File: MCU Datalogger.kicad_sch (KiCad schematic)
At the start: 25 parts, among them U1 24LC1025, U2 24LC1025, U3 ATMEGA328P-AU, U4 DS1337S_, Y1 32.768kHz, Y2 16KHz

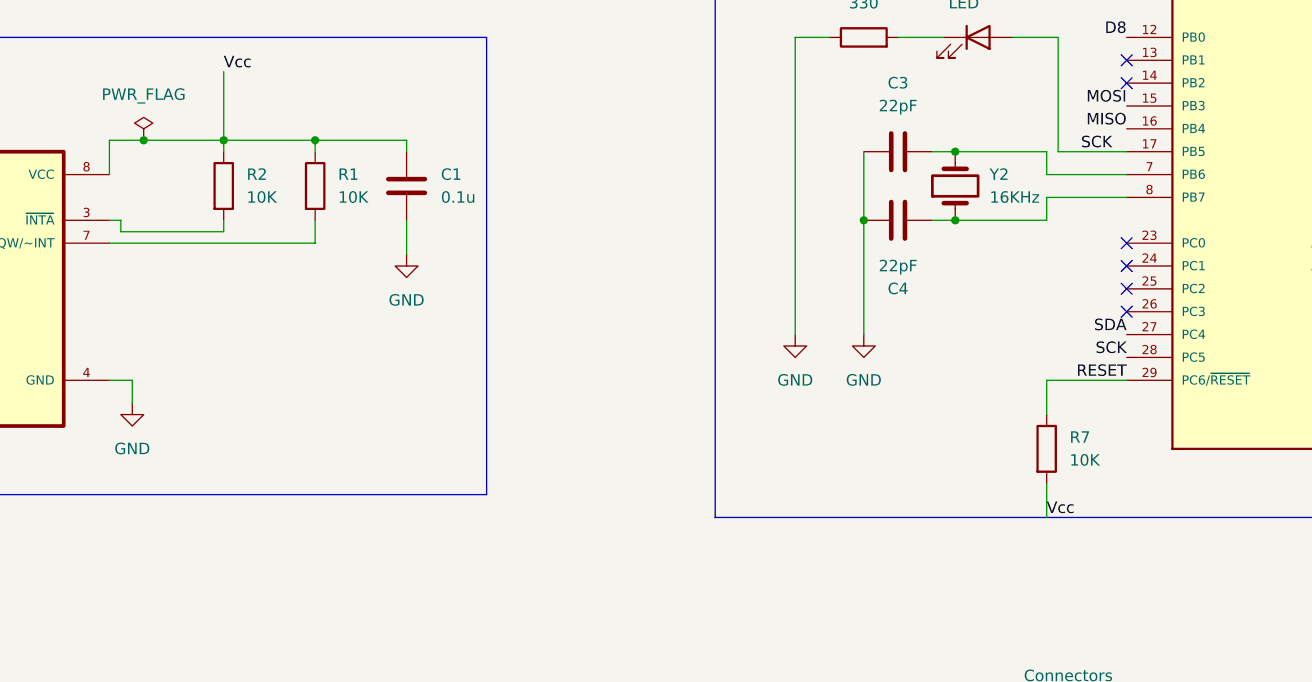
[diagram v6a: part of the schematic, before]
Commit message: completed the routing of the PCB
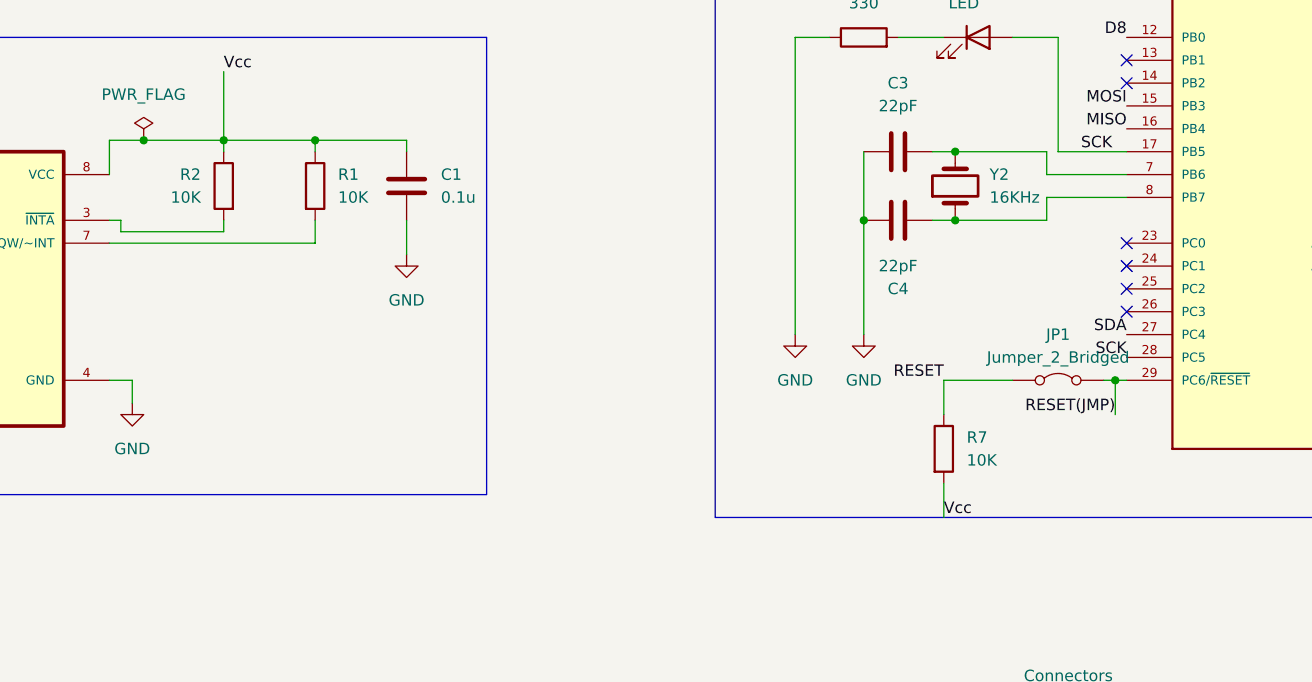
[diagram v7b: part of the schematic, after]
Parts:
- added JP1: Jumper_2_Bridged, Resistor_SMD:R_1206_3216Metric_Pad1.30x1.75mm_HandSolder, symbol Jumper:Jumper_2_Bridged
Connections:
- net RESET: now also JP1.2 (B); no longer U3.29 (PC6/~{RESET})
- new net RESET(JMP): JP1.1 (A), U3.29 (PC6/~{RESET})
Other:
- moved on the sheet: R7
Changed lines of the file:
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@@
 	)
 	(junction
+		(at 199.39 81.28)
+		(diameter 0)
+		(color 0 0 0 0)
+	)
+	(junction
 		(at 273.05 57.15)
 		(diameter 0)
@@
 	(wire
 		(pts
-			(xy 191.77 81.28) (xy 191.77 85.09)
-		)
-		(stroke
-			(width 0)
-			(type default)
-		)
-	)
-	(wire
-		(pts
 			(xy 124.46 151.13) (xy 130.81 151.13)
 		)
@@
 	(wire
 		(pts
+			(xy 199.39 81.28) (xy 200.66 81.28)
+		)
+		(stroke
+			(width 0)
+			(type default)
+		)
+	)
+	(wire
+		(pts
 			(xy 171.45 119.38) (xy 171.45 123.19)
 		)
@@
 	(wire
 		(pts
+			(xy 180.34 81.28) (xy 180.34 85.09)
+		)
+		(stroke
+			(width 0)
+			(type default)
+		)
+	)
+	(wire
+		(pts
 			(xy 181.61 63.5) (xy 191.77 63.5)
 		)
@@
 	(wire
 		(pts
+			(xy 198.12 81.28) (xy 199.39 81.28)
+		)
+		(stroke
+			(width 0)
+			(type default)
+		)
+	)
+	(wire
+		(pts
 			(xy 231.14 86.36) (xy 238.76 86.36)
 		)
@@
 	(wire
 		(pts
-			(xy 191.77 92.71) (xy 191.77 96.52)
+			(xy 180.34 92.71) (xy 180.34 96.52)
 		)
 		(stroke
@@
 	(wire
 		(pts
+			(xy 199.39 85.09) (xy 199.39 81.28)
+		)
+		(stroke
+			(width 0)
+			(type default)
+		)
+	)
+	(wire
+		(pts
 			(xy 273.05 86.36) (xy 273.05 57.15)
 		)
@@
 	(wire
 		(pts
+			(xy 187.96 81.28) (xy 180.34 81.28)
+		)
+		(stroke
+			(width 0)
+			(type default)
+		)
+	)
+	(wire
+		(pts
 			(xy 181.61 55.88) (xy 191.77 55.88)
 		)
@@
 	(wire
 		(pts
-			(xy 200.66 81.28) (xy 191.77 81.28)
-		)
-		(stroke
-			(width 0)
-			(type default)
-		)
-	)
-	(wire
-		(pts
 			(xy 90.17 81.28) (xy 90.17 83.82)
 		)
@@
 		)
 	)
-	(label "D8"
-		(at 200.66 43.18 180)
+	(label "RESET(JMP)"
+		(at 199.39 85.09 180)
 		(fields_autoplaced yes)
 		(effects
@@
 		)
 	)
-	(label "Vcc"
-		(at 191.77 96.52 0)
+	(label "D8"
+		(at 200.66 43.18 180)
 		(fields_autoplaced yes)
 		(effects
@@
 				(size 1.27 1.27)
 			)
-			(justify left bottom)
+			(justify right bottom)
 		)
 	)
-	(label "RESET"
-		(at 200.66 81.28 180)
+	(label "Vcc"
+		(at 180.34 96.52 0)
 		(fields_autoplaced yes)
 		(effects
@@
 				(size 1.27 1.27)
 			)
-			(justify right bottom)
+			(justify left bottom)
 		)
 	)
@@
 		)
 	)
+	(label "RESET"
+		(at 180.34 81.28 180)
+		(fields_autoplaced yes)
+		(effects
+			(font
+				(size 1.27 1.27)
+			)
+			(justify right bottom)
+		)
+	)
 	(label "Vcc"
 		(at 92.71 149.86 0)
@@
 	(symbol
 		(lib_id "Device:R")
-		(at 191.77 88.9 0)
+		(at 180.34 88.9 0)
 		(unit 1)
 		(exclude_from_sim no)
@@
 		(fields_autoplaced yes)
 		(property "Reference" "R7"
-			(at 194.31 87.6299 0)
+			(at 182.88 87.6299 0)
 			(effects
 				(font
@@
 		)
 		(property "Value" "10K"
-			(at 194.31 90.1699 0)
+			(at 182.88 90.1699 0)
 			(effects
 				(font
@@
 		)
 		(property "Footprint" "Resistor_SMD:R_0805_2012Metric_Pad1.20x1.40mm_HandSolder"
-			(at 189.992 88.9 90)
+			(at 178.562 88.9 90)
 			(effects
 				(font
@@
 		)
 		(property "Datasheet" "~"
-			(at 191.77 88.9 0)
+			(at 180.34 88.9 0)
 			(effects
 				(font
@@
 		)
 		(property "Description" "Resistor"
-			(at 191.77 88.9 0)
+			(at 180.34 88.9 0)
 			(effects
 				(font
@@
 		)
 		(property "descrisc" ""
-			(at 191.77 88.9 0)
+			(at 180.34 88.9 0)
 			(effects
 				(font
@@
 		(lib_id "Device:R")
 		(at 100.33 59.69 0)
+		(mirror y)
 		(unit 1)
 		(exclude_from_sim no)
@@
 		(on_board yes)
 		(dnp no)
-		(fields_autoplaced yes)
 		(property "Reference" "R2"
-			(at 102.87 58.4199 0)
+			(at 97.79 58.4199 0)
 			(effects
 				(font
@@
 		)
 		(property "Value" "10K"
-			(at 102.87 60.9599 0)
+			(at 97.79 60.9599 0)
 			(effects
 				(font
@@
 		)
 		(property "Footprint" "Resistor_SMD:R_0805_2012Metric_Pad1.20x1.40mm_HandSolder"
-			(at 98.552 59.69 90)
+			(at 102.108 59.69 90)
 			(effects
 				(font
@@
 					(unit 1)
 				)
+			)
+		)
+	)
+	(symbol
+		(lib_id "Jumper:Jumper_2_Bridged")
+		(at 193.04 81.28 0)
+		(mirror y)
+		(unit 1)
+		(exclude_from_sim yes)
+		(in_bom yes)
+		(on_board yes)
+		(dnp no)
+		(property "Reference" "JP1"
+			(at 193.04 76.2 0)
+			(effects
+				(font
+					(size 1.27 1.27)
+				)
+			)
+		)
+		(property "Value" "Jumper_2_Bridged"
+			(at 193.04 78.74 0)
+			(effects
+				(font
+					(size 1.27 1.27)
+				)
+			)
+		)
+		(property "Footprint" "Resistor_SMD:R_1206_3216Metric_Pad1.30x1.75mm_HandSolder"
+			(at 193.04 81.28 0)
+			(effects
+				(font
+					(size 1.27 1.27)
+				)
+				(hide yes)
+			)
+		)
+		(property "Datasheet" "~"
+			(at 193.04 81.28 0)
+			(effects
+				(font
+					(size 1.27 1.27)
+				)
+				(hide yes)
+			)
+		)
+		(property "Description" "Jumper, 2-pole, closed/bridged"
+			(at 193.04 81.28 0)
+			(effects
+				(font
+					(size 1.27 1.27)
+				)
+				(hide yes)
+			)
+		)
+		(property "descrisc" ""
+			(at 193.04 81.28 0)
+			(effects
+				(font
+					(size 1.27 1.27)
+				)
+				(hide yes)
+			)
+		)
+		(pin "2"
+		)
+		(pin "1"
+		)
+		(instances
+			(project ""
+				(path "/2d095fec-de04-4caa-8a5d-d4c981edd86b"
+					(reference "JP1")
+					(unit 1)
+				)

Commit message: fixed some issues with the EEPROM footprint 3d models
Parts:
- U1, U2: footprint Package_SO:SOIC-8_5.23x5.23mm_P1.27mm -> Package_SO:SOIC-8_5.275x5.275mm_P1.27mm
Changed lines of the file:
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@@
 			)
 		)
-		(property "Footprint" "Package_SO:SOIC-8_5.23x5.23mm_P1.27mm"
+		(property "Footprint" "Package_SO:SOIC-8_5.275x5.275mm_P1.27mm"
 			(at 92.71 157.48 0)
 			(effects
@@
 		)
 		(property "Description" "I2C Serial EEPROM, 1024Kb, DIP-8/SOIC-8/TSSOP-8/DFN-8"
+			(at 92.71 157.48 0)
+			(effects
+				(font
+					(size 1.27 1.27)
+				)
+				(hide yes)
+			)
+		)
+		(property "descrisc" ""
 			(at 92.71 157.48 0)
 			(effects
@@
 			)
 		)
-		(property "Footprint" "Package_SO:SOIC-8_5.23x5.23mm_P1.27mm"
+		(property "Footprint" "Package_SO:SOIC-8_5.275x5.275mm_P1.27mm"
 			(at 52.07 157.48 0)
 			(effects
@@
 			(at 52.07 157.48 0)
 			(effects
+				(font
+					(size 1.27 1.27)
+				)
+				(hide yes)
+			)
+		)
+		(property "descrisc" ""
+			(at 52.07 157.48 0)
+			(effects
